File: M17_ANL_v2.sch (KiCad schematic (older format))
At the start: 108 parts, among them IC1 ADF7021, J1 USB_A, J2 RF_PORT, J3 Conn_01x05, J4 Conn_01x05, U1 STM32F303CBTx, U2 AP1117-33, X1 ASV-xxxMHz, X2 ASV-xxxMHz

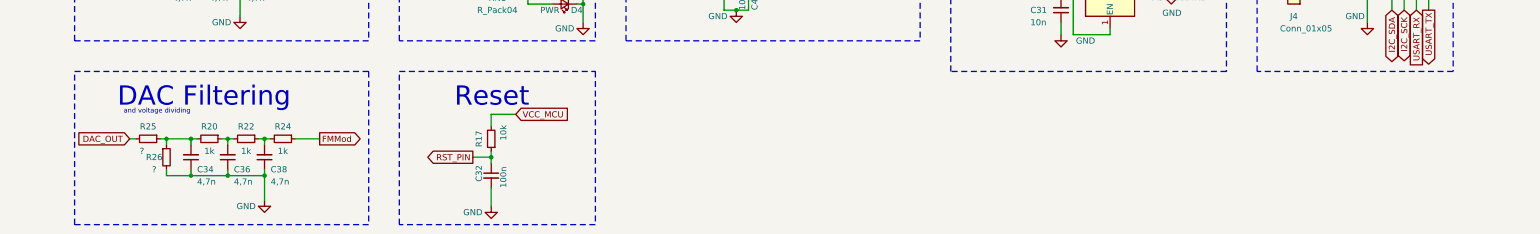
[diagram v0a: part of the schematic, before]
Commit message: Added information about R25 and R26 with no value yet
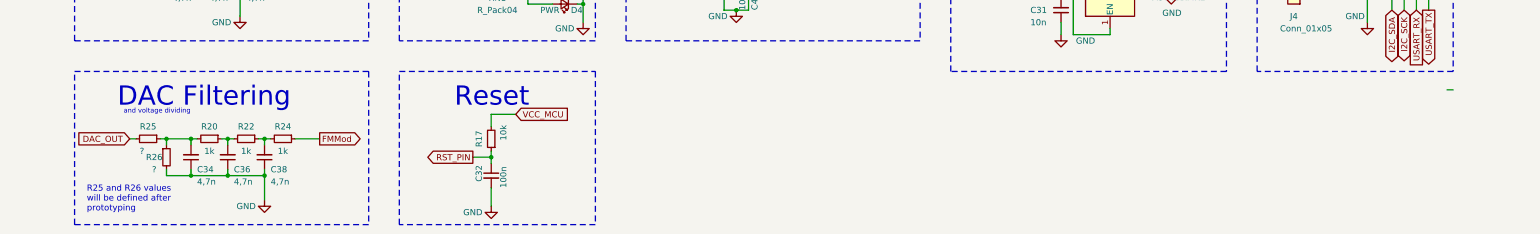
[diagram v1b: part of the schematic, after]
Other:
- note added: "R25 and R26 values\nwill be defined after\nprototyping"
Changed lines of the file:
@@
 Wire Wire Line
 	7250 7850 7350 7850
+Wire Wire Line
+	13100 8500 13050 8500
+Text Notes 1950 9500 0    50   ~ 0
+R25 and R26 values\nwill be defined after\nprototyping
 $EndSCHEMATC

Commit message: added choke for radio part of M17_ANL_v2 added choke of input and output of the voltage regulator
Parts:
- removed J4: Conn_01x05, Connector_PinHeader_1.27mm:PinHeader_1x05_P1.27mm_Vertical, symbol Connector_Generic:Conn_01x05
- added C44: 100n, Capacitor_SMD:C_0603_1608Metric, symbol Device:C_Small
- added C45: 100n, Capacitor_SMD:C_0805_2012Metric, symbol Device:C_Small
- added J4: Conn_01x06, Connector_PinHeader_1.27mm:PinHeader_1x06_P1.27mm_Vertical, symbol Connector_Generic:Conn_01x06
- added L6, L8: 10uH, Inductor_SMD:L_0805_2012Metric, symbol Device:L_Small
- added L7: 1uH, Inductor_SMD:L_0805_2012Metric, symbol Device:L_Small
- C31: footprint Capacitor_SMD:C_0603_1608Metric -> Capacitor_SMD:C_0402_1005Metric
- C41: value 10n -> 1n; footprint Capacitor_SMD:C_0805_2012Metric -> Capacitor_SMD:C_0603_1608Metric
- C42, C43: footprint Capacitor_SMD:C_0805_2012Metric -> Capacitor_SMD:C_0603_1608Metric
- J3: value Conn_01x05 -> PROG
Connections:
- wire segments 485 -> 499
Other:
- moved on the sheet: C1, C17, C18, C19, C6, R30, U2

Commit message: Plotted new PDF of schematic
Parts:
- renumbered IC1 to U2, U2 to U3
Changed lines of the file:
@@
 Power converter
 $Comp
-L Regulator_Linear:AP1117-33 U2
+L Regulator_Linear:AP1117-33 U3
 U 1 1 5E3092A8
 P 7350 5900
-F 0 "U2" H 7350 6142 50  0000 C CNN
+F 0 "U3" H 7350 6142 50  0000 C CNN
 F 1 "AP1117-33" H 7350 6051 50  0000 C CNN
 F 2 "Package_TO_SOT_SMD:SOT-223-3_TabPin2" H 7350 6100 50  0001 C CNN
@@
 	8350 3650 8150 3650
 $Comp
-L RFElements:ADF7021-VBCPZ-RL IC1
+L RFElements:ADF7021-VBCPZ-RL U2
 U 1 1 5DF32167
 P 10750 3100
-F 0 "IC1" H 11650 2000 50  0000 L CNN
+F 0 "U2" H 11650 2000 50  0000 L CNN
 F 1 "ADF7021" H 11550 1900 50  0000 L CNN
 F 2 "RFElements:ADF7021" H 12400 3600 50  0001 L CNN

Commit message: Readme header description added
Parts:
- added C46: 1n, Capacitor_SMD:C_0603_1608Metric, symbol Device:C_Small
- added R31: 47k, Resistor_SMD:R_0402_1005Metric, symbol Device:R_Small
- added R32: 100, Resistor_SMD:R_0402_1005Metric, symbol Device:R_Small
- R24: value 1k -> 100k
- R25, R26: value ? -> 1k
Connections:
- wire segments 499 -> 507
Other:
- moved on the sheet: C14, C15, C16, C33, C35, C37, C40, R11, R12, R19, R21, R23
